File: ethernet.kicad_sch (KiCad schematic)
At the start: 46 parts, among them U1 MPFS250T-FCVG484, U16 DP83867ISRGZR, Y2 Resonator_25MHz_ABM8G

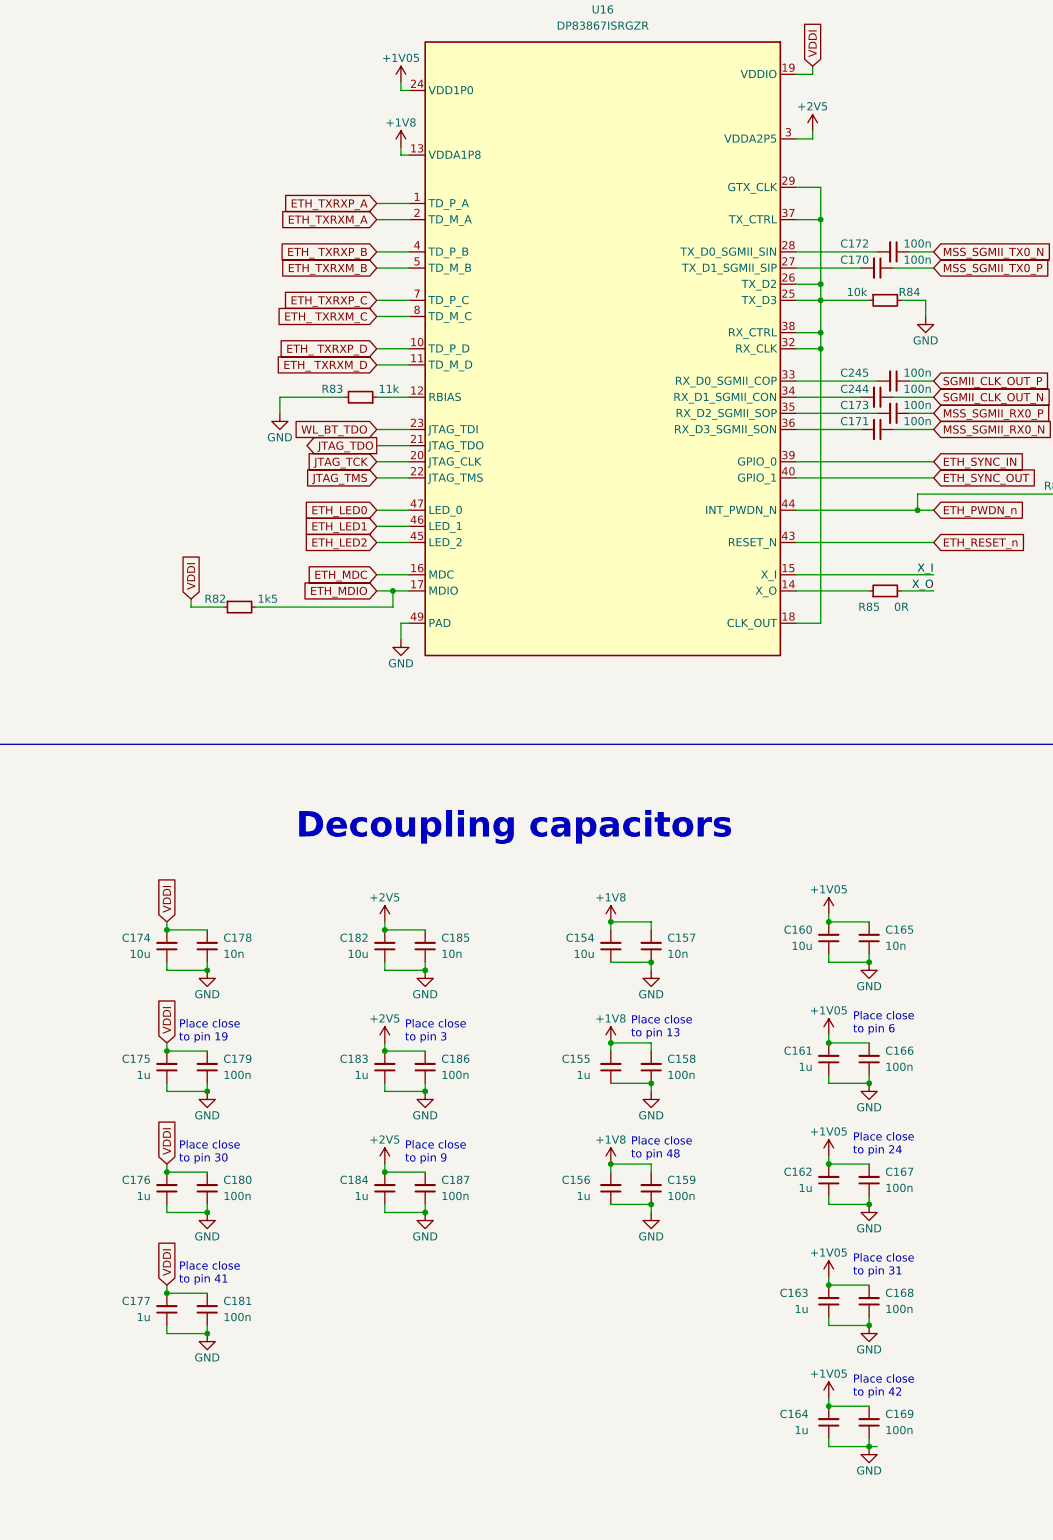
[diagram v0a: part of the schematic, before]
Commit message: [#54899] Change Ethernet PHY power configuration to Two-Supply
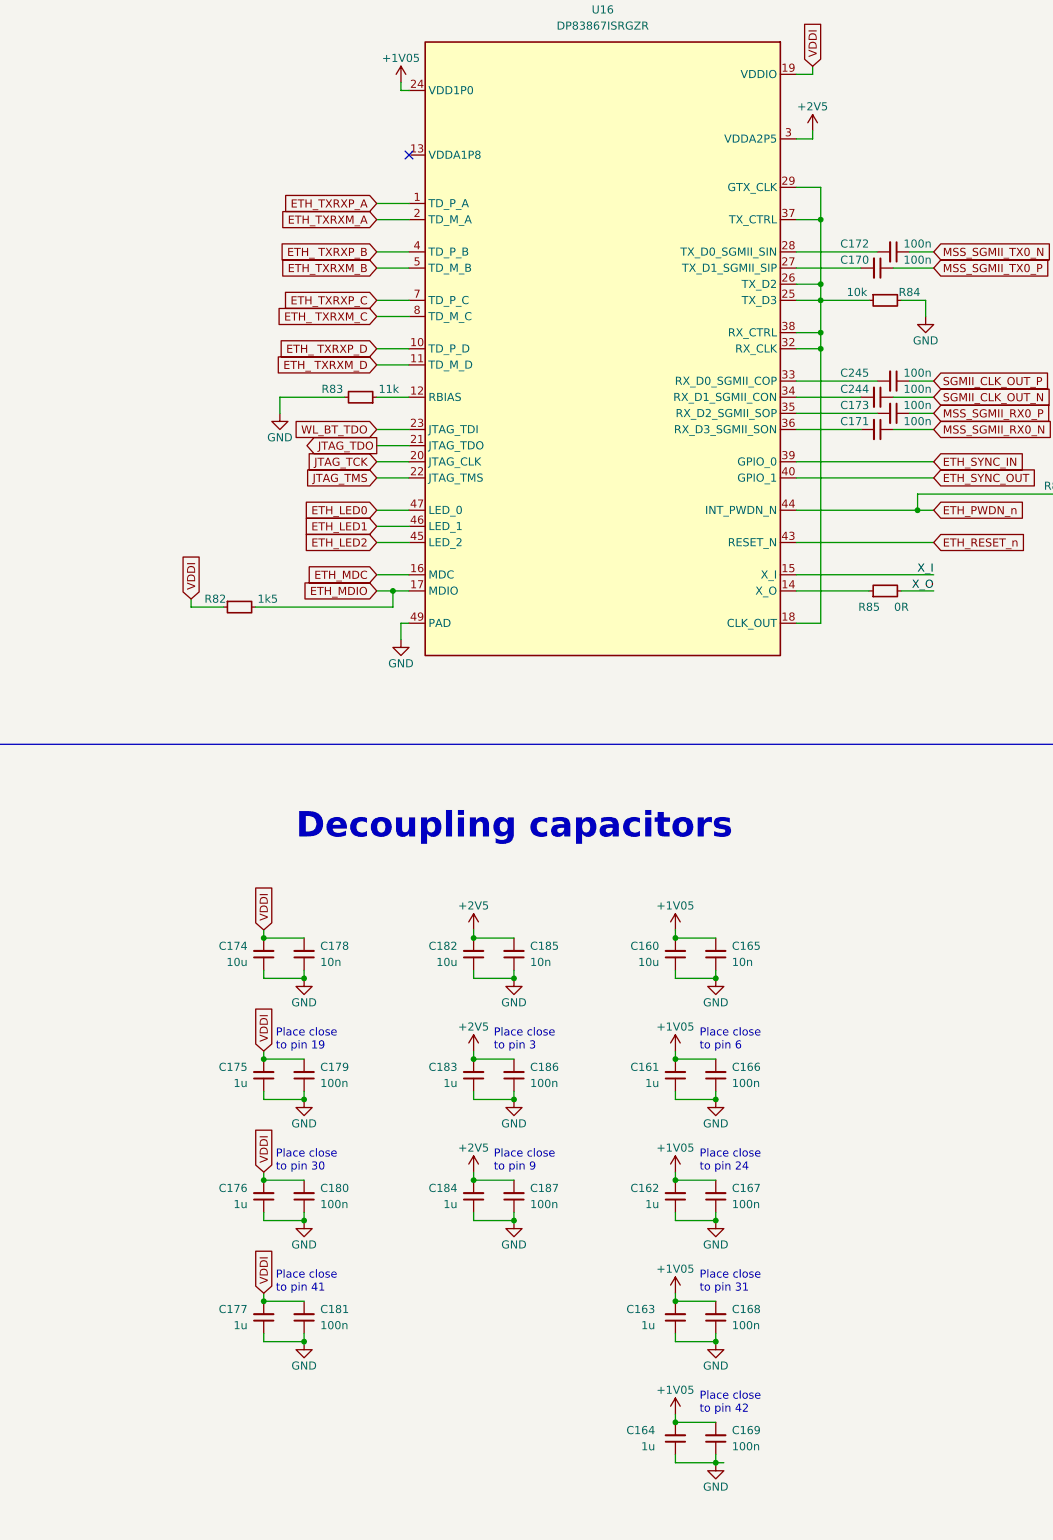
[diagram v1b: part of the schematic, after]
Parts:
- removed C154: C_10u_0402, antmicro-footprints:C_0402_1005Metric, symbol antmicroCapacitors0402:C_10u_0402
- removed C155, C156: C_1u_0402, antmicro-footprints:C_0402_1005Metric, symbol antmicroCapacitors0402:C_1u_0402
- removed C157: C_10n_0402, antmicro-footprints:C_0402_1005Metric, symbol antmicroCapacitors0402:C_10n_0402
- removed C158, C159: C_100n_0201_25V, antmicro-footprints:C_0201, symbol antmicroCapacitorsmisc:C_100n_0201_25V
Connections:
- net +1V8: no longer names the net of U16.13 (VDDA1P8), U16.48 (VDDA1P8)
- no-connect marks 4 -> 5
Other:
- note removed: "Place close to pin 13"
- note removed: "Place close to pin 48"
- moved on the sheet: C160, C161, C162, C163, C164, C165, C166, C167, C168, C169, C174, C175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

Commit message: [#54899] Re-annotate components
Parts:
- renumbered C174 to C250, C175 to C251, C176 to C252, C177 to C253, C178 to C254, C179 to C255, C180 to C256, C181 to C257, C182 to C258, C183 to C259, C184 to C260, C185 to C261, C186 to C262, C187 to C263, C160 to C264, C161 to C265, C162 to C266, C163 to C267, C164 to C268, C165 to C269, C166 to C270, C167 to C271, C168 to C272, C169 to C273, C170 to C274, C244 to C275, C171 to C276, C172 to C277, C245 to C278, C173 to C279, C246 to C280, C247 to C281, R82 to R137, R83 to R138, R84 to R139, R85 to R140, R86 to R141, U16 to U25, Y2 to Y3

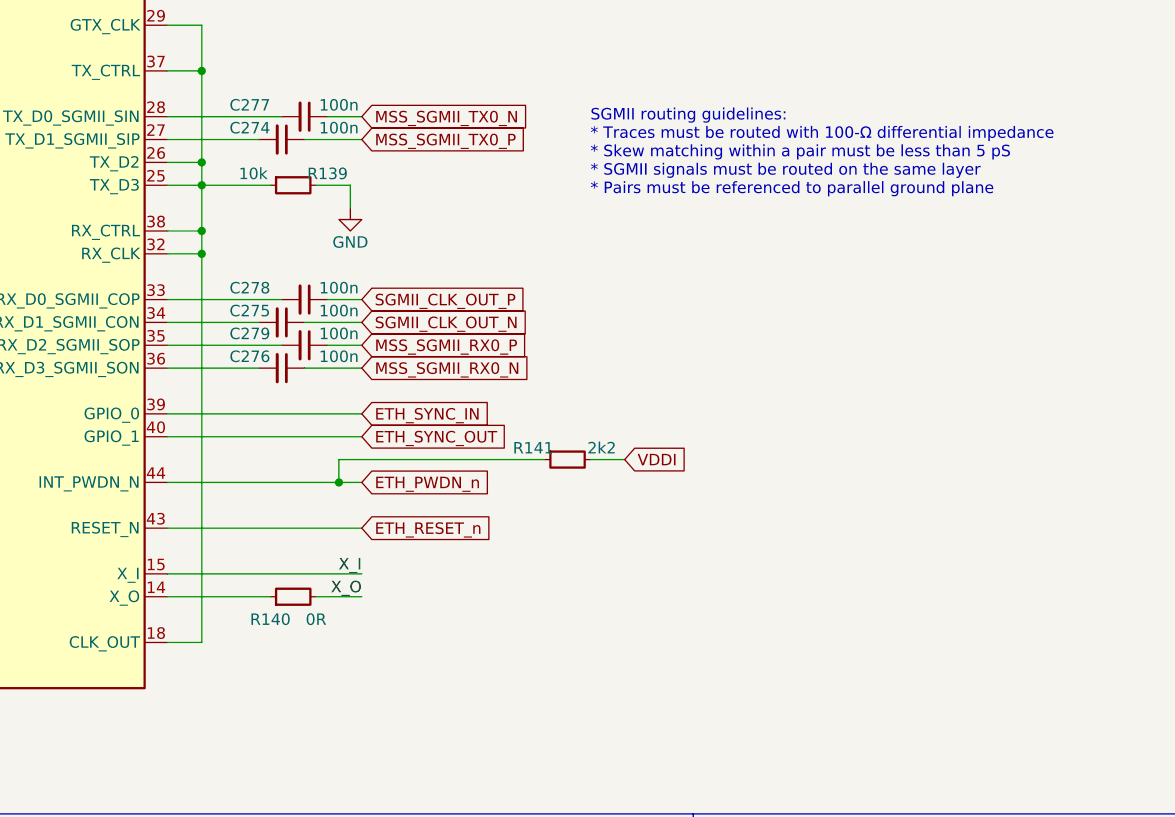
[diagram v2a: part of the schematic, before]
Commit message: [#54899] Connect unused Ethernet PHY pins according to reference design
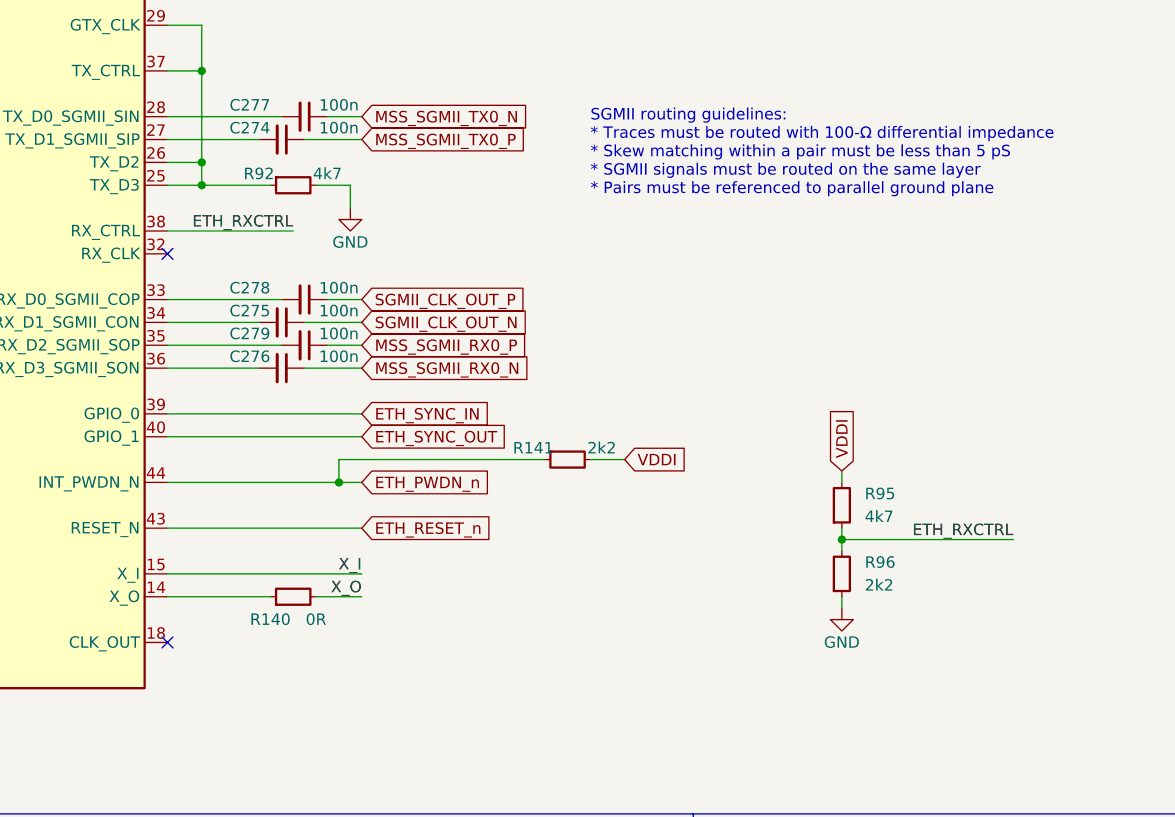
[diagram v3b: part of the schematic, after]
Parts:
- removed R139: R_10k_0402, antmicro-footprints:R_0402_1005Metric, symbol antmicroResistors0402:R_10k_0402
- added R92, R95: R_4k7_0402, antmicro-footprints:R_0402_1005Metric, symbol antmicroResistors0402:R_4k7_0402
- added R96: R_2k2_0402, antmicro-footprints:R_0402_1005Metric, symbol antmicroResistors0402:R_2k2_0402
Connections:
- net GND: now also R92.2, R96.1
- net VDDI: now also R95.2
- net at U25.25 (TX_D3), U25.26 (TX_D2), U25.29 (GTX_CLK)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: now also R92.1; no longer U25.18 (CLK_OUT), U25.32 (RX_CLK), U25.38 (RX_CTRL)
- new net ETH_RXCTRL: R95.1, R96.2, U25.38 (RX_CTRL)
- no-connect marks 5 -> 7

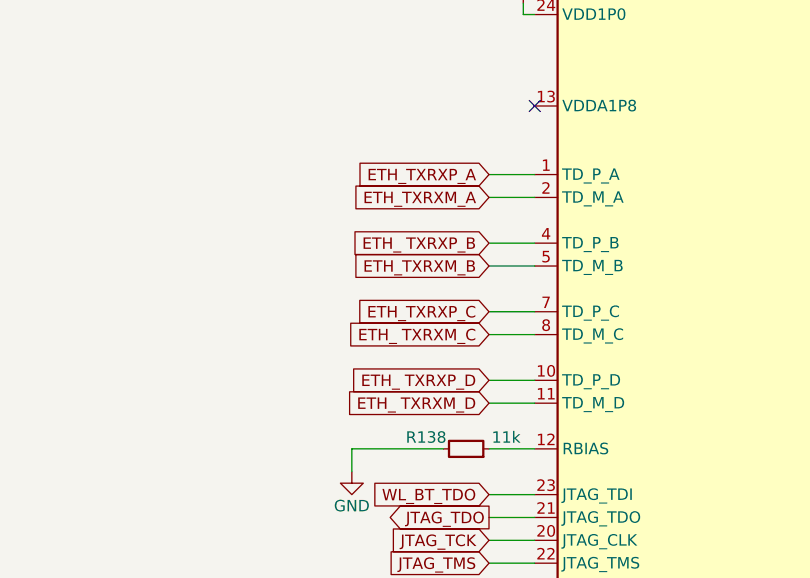
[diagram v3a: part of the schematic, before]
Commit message: [#54899] Change ETH labels to differential
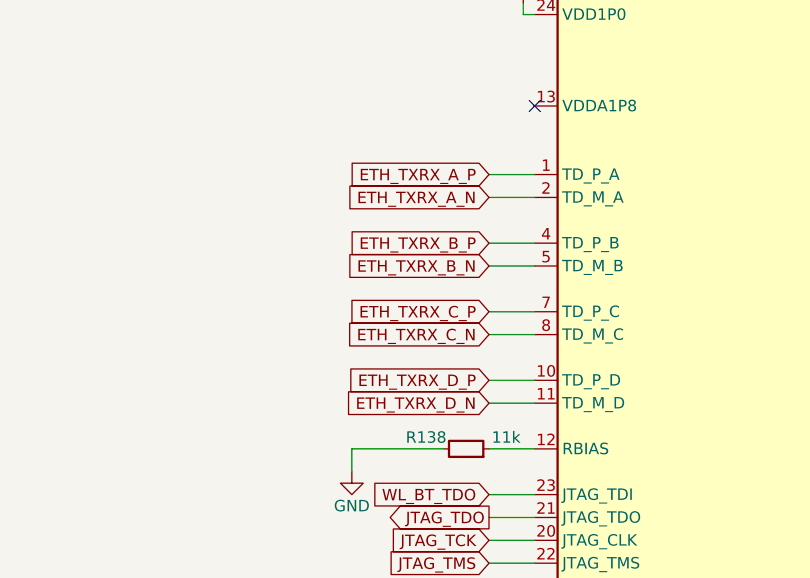
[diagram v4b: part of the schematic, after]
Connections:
- net ETH_ TXRXM_C renamed ETH_TXRX_C_N
- net ETH_ TXRXM_D renamed ETH_TXRX_D_N
- net ETH_ TXRXP_B renamed ETH_TXRX_B_P
- net ETH_ TXRXP_D renamed ETH_TXRX_D_P
- net ETH_TXRXM_A renamed ETH_TXRX_A_N
- net ETH_TXRXM_B renamed ETH_TXRX_B_N
- net ETH_TXRXP_A renamed ETH_TXRX_A_P
- net ETH_TXRXP_C renamed ETH_TXRX_C_P
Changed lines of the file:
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@@
     )
   )
-  (global_label "ETH_TXRXM_B" (shape input) (at 86.36 85.09 180) (fields_autoplaced)
-    (effects (font (size 1.27 1.27)) (justify right))
-    (property "Intersheetrefs" "${INTERSHEET_REFS}" (at 71.1864 85.0106 0)
+  (global_label "ETH_TXRX_B_N" (shape input) (at 86.36 85.09 180) (fields_autoplaced)
+    (effects (font (size 1.27 1.27)) (justify right))
+    (property "Intersheetrefs" "${INTERSHEET_REFS}" (at 69.7678 85.09 0)
       (effects (font (size 1.27 1.27)) (justify right) hide)
     )
@@
     )
   )
-  (global_label "ETH_TXRXP_C" (shape input) (at 86.36 90.17 180) (fields_autoplaced)
-    (effects (font (size 1.27 1.27)) (justify right))
-    (property "Intersheetrefs" "${INTERSHEET_REFS}" (at 71.3679 90.0906 0)
+  (global_label "ETH_TXRX_C_P" (shape input) (at 86.36 90.17 180) (fields_autoplaced)
+    (effects (font (size 1.27 1.27)) (justify right))
+    (property "Intersheetrefs" "${INTERSHEET_REFS}" (at 69.8283 90.17 0)
       (effects (font (size 1.27 1.27)) (justify right) hide)
     )
@@
     )
   )
-  (global_label "ETH_TXRXP_A" (shape input) (at 86.36 74.93 180) (fields_autoplaced)
-    (effects (font (size 1.27 1.27)) (justify right))
-    (property "Intersheetrefs" "${INTERSHEET_REFS}" (at 71.5493 74.8506 0)
-      (effects (font (size 1.27 1.27)) (justify right) hide)
-    )
-  )
-  (global_label "ETH_ TXRXP_B" (shape input) (at 86.36 82.55 180) (fields_autoplaced)
-    (effects (font (size 1.27 1.27)) (justify right))
-    (property "Intersheetrefs" "${INTERSHEET_REFS}" (at 70.4002 82.4706 0)
+  (global_label "ETH_TXRX_A_P" (shape input) (at 86.36 74.93 180) (fields_autoplaced)
+    (effects (font (size 1.27 1.27)) (justify right))
+    (property "Intersheetrefs" "${INTERSHEET_REFS}" (at 70.0097 74.93 0)
+      (effects (font (size 1.27 1.27)) (justify right) hide)
+    )
+  )
+  (global_label "ETH_TXRX_B_P" (shape input) (at 86.36 82.55 180) (fields_autoplaced)
+    (effects (font (size 1.27 1.27)) (justify right))
+    (property "Intersheetrefs" "${INTERSHEET_REFS}" (at 69.8283 82.55 0)
       (effects (font (size 1.27 1.27)) (justify right) hide)
     )
@@
     )
   )
-  (global_label "ETH_TXRXM_A" (shape input) (at 86.36 77.47 180) (fields_autoplaced)
-    (effects (font (size 1.27 1.27)) (justify right))
-    (property "Intersheetrefs" "${INTERSHEET_REFS}" (at 71.3679 77.3906 0)
+  (global_label "ETH_TXRX_A_N" (shape input) (at 86.36 77.47 180) (fields_autoplaced)
+    (effects (font (size 1.27 1.27)) (justify right))
+    (property "Intersheetrefs" "${INTERSHEET_REFS}" (at 69.9492 77.47 0)
       (effects (font (size 1.27 1.27)) (justify right) hide)
     )
@@
     )
   )
-  (global_label "ETH_ TXRXP_D" (shape input) (at 86.36 97.79 180) (fields_autoplaced)
-    (effects (font (size 1.27 1.27)) (justify right))
-    (property "Intersheetrefs" "${INTERSHEET_REFS}" (at 70.4002 97.7106 0)
+  (global_label "ETH_TXRX_D_P" (shape input) (at 86.36 97.79 180) (fields_autoplaced)
+    (effects (font (size 1.27 1.27)) (justify right))
+    (property "Intersheetrefs" "${INTERSHEET_REFS}" (at 69.8283 97.79 0)
       (effects (font (size 1.27 1.27)) (justify right) hide)
     )
@@
     )
   )
-  (global_label "ETH_ TXRXM_C" (shape input) (at 86.36 92.71 180) (fields_autoplaced)
-    (effects (font (size 1.27 1.27)) (justify right))
-    (property "Intersheetrefs" "${INTERSHEET_REFS}" (at 70.2188 92.6306 0)
+  (global_label "ETH_TXRX_C_N" (shape input) (at 86.36 92.71 180) (fields_autoplaced)
+    (effects (font (size 1.27 1.27)) (justify right))
+    (property "Intersheetrefs" "${INTERSHEET_REFS}" (at 69.7678 92.71 0)
       (effects (font (size 1.27 1.27)) (justify right) hide)
     )
@@
     )
   )
-  (global_label "ETH_ TXRXM_D" (shape input) (at 86.36 100.33 180) (fields_autoplaced)
-    (effects (font (size 1.27 1.27)) (justify right))
-    (property "Intersheetrefs" "${INTERSHEET_REFS}" (at 70.2188 100.2506 0)
-      (effects (font (size 1.27 1.27)) (justify right) hide)
-    )
+  (global_label "ETH_TXRX_D_N" (shape input) (at 86.36 100.33 180) (fields_autoplaced)
+    (effects (font (size 1.27 1.27)) (justify right))
+    (property "Intersheetrefs" "${INTERSHEET_REFS}" (at 69.7678 100.33 0)
+      (effects (font (size 1.27 1.27)) (justify right) hide)
+    )

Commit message: [#54899] Update symbols
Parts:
- U1: footprint antmicro-footprints:BGA-484_19x19mm_Layout22x22_P0.8mm_FCVG484 -> antmicro-footprints:BGA-484_19x19mm_Layout22x22_P0.8mm_MPFS250T-FCVG484
- U25: Manufacturer (none) -> Texas Instruments
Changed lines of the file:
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@@
       (effects (font (size 1.27 1.27) (thickness 0.15)))
+    )
+    (property "Manufacturer" "Texas Instruments" (at 76.2 67.31 0)
+      (effects (font (size 1.27 1.27)) (justify left bottom) hide)
     )
     (pin "1")
@@
       (effects (font (size 1.27 1.27) (thickness 0.15)) (justify left bottom) hide)
     )
-    (property "Footprint" "antmicro-footprints:BGA-484_19x19mm_Layout22x22_P0.8mm_FCVG484" (at 382.27 218.44 0)
-      (effects (font (size 1.27 1.27) (thickness 0.15)) (justify left bottom) hide)
-    )
+    (property "Footprint" "antmicro-footprints:BGA-484_19x19mm_Layout22x22_P0.8mm_MPFS250T-FCVG484" (at 382.27 218.44 0)
+      (effects (font (size 1.27 1.27) (thickness 0.15)) (justify left bottom) hide)
+    )
